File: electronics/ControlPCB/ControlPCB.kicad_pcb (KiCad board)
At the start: 2 copper layers, 119.6 x 90.4 mm, 44 parts, among them CON1 12VINPUT, P1 Opto1, P2 Opto2, P3 Opto3, P4 Opto4, P5 Opto5, P6 Opto6, P7 Tool, U1 POLOLU_A4988, U2 POLOLU_A4988, U3 POLOLU_A4988, U4 POLOLU_A4988, U5 POLOLU_A4988, U6 POLOLU_A4988, U7 POLOLU_A4988

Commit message: PCB update
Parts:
- removed REF**: Symbol_OSHW-Logo_CopperTop_BIG, Symbols:Symbol_OSHW-Logo_CopperTop_BIG
- removed REF** (x4): 1pin, Connect:1pin
- added C8: CP1_Small, Capacitors_SMD:c_elec_6.3x5.7, F.Cu at (166.6, 91.4)
- added D1: D_Small, Diodes_ThroughHole:Diode_DO-35_SOD27_Horizontal_RM10, F.Cu at (85.3, 91.2)
- added DLED1: LEDFAN, LEDs:LED_1206, F.Cu at (100.7, 54.2)
- added DLED2: LED12V, LEDs:LED_1206, F.Cu at (93.3, 54.2)
- added DLED3: LED5V, LEDs:LED_1206, F.Cu at (107.8, 54.2)
- added F1: F_Small, Fuse_Holders_and_Fuses:Fuse_TE5_Littlefuse-395Series, F.Cu at (81.0, 96.0)
- added P8: CONN_02X03, Pin_Headers:Pin_Header_Straight_2x03, F.Cu at (158.8, 87.6)
- added PM8: CONN_01X04, Pin_Headers:Pin_Header_Straight_1x04, F.Cu at (165.1, 100.6)
- added PS1: Opto1, Pin_Headers:Pin_Header_Straight_1x03, F.Cu at (141.4, 49.9)
- added PS2: Opto2, Pin_Headers:Pin_Header_Straight_1x03, F.Cu at (144.9, 49.9)
- added PS3: Opto3, Pin_Headers:Pin_Header_Straight_1x03, F.Cu at (148.5, 49.9)
- added PS4: Opto4, Pin_Headers:Pin_Header_Straight_1x03, F.Cu at (152.0, 49.9)
- added PS5: Opto5, Pin_Headers:Pin_Header_Straight_1x03, F.Cu at (155.6, 49.9)
- added PS6: Opto6, Pin_Headers:Pin_Header_Straight_1x03, F.Cu at (159.1, 49.9)
- added PS7: Opto7, Pin_Headers:Pin_Header_Straight_1x03, F.Cu at (162.7, 49.9)
- added PS8: Opto8, Pin_Headers:Pin_Header_Straight_1x03, F.Cu at (166.2, 49.9)
- added PSW1: CONN_01X02, Connect:AK300-2, F.Cu at (82.8, 84.3)
- added PT1: Tool, Pin_Headers:Pin_Header_Straight_1x03, F.Cu at (169.8, 49.9)
- added R10: R, Resistors_SMD:R_1206_HandSoldering, F.Cu at (117.1, 72.1)
- added R11: R, Resistors_SMD:R_1206_HandSoldering, F.Cu at (137.4, 72.1)
- added R12: R, Resistors_SMD:R_1206_HandSoldering, F.Cu at (157.7, 72.1)
- added R13: R, Resistors_SMD:R_1206_HandSoldering, F.Cu at (96.8, 93.7)
- added R14: R, Resistors_SMD:R_1206_HandSoldering, F.Cu at (117.1, 93.7)
- added R15: R, Resistors_SMD:R_1206_HandSoldering, F.Cu at (137.4, 93.7)
- added R16: R, Resistors_SMD:R_1206_HandSoldering, F.Cu at (157.7, 93.7)
- added R8: R, Resistors_SMD:R_1206_HandSoldering, F.Cu at (167.6, 86.4)
- added R9: R, Resistors_SMD:R_1206_HandSoldering, F.Cu at (96.8, 72.1)
- added RLED1: 560, Resistors_SMD:R_1206_HandSoldering, F.Cu at (100.7, 50.7)
- added RLED2: 560, Resistors_SMD:R_1206_HandSoldering, F.Cu at (93.3, 50.7)
- added RLED3: 220, Resistors_SMD:R_1206_HandSoldering, F.Cu at (107.8, 50.7)
- added U8: POLOLU_A4988, Pololu:SWDIP8_.6W, F.Cu at (161.3, 90.2)
- C1, C2, C3, C4, C5, C6, C7: footprint POL:C_Radial_D6.3_L11.2_P2.5THOR -> Capacitors_SMD:c_elec_6.3x5.7
- P1: value Opto1 -> CONN_02X03; footprint Pin_Header_Straight_1x03 -> Pin_Headers:Pin_Header_Straight_2x03
- P2: value Opto2 -> CONN_02X03; footprint POL:Pin_Header_Straight_1x03 -> Pin_Headers:Pin_Header_Straight_2x03
- P3: value Opto3 -> CONN_02X03; footprint POL:Pin_Header_Straight_1x03 -> Pin_Headers:Pin_Header_Straight_2x03
- P4: value Opto4 -> CONN_02X03; footprint POL:Pin_Header_Straight_1x03 -> Pin_Headers:Pin_Header_Straight_2x03
- P5: value Opto5 -> CONN_02X03; footprint POL:Pin_Header_Straight_1x03 -> Pin_Headers:Pin_Header_Straight_2x03
- P6: value Opto6 -> CONN_02X03; footprint POL:Pin_Header_Straight_1x03 -> Pin_Headers:Pin_Header_Straight_2x03
- P7: value Tool -> CONN_02X03; footprint POL:Pin_Header_Straight_1x03 -> Pin_Headers:Pin_Header_Straight_2x03
- PA1: footprint POL:Pin_Header_Straight_2x03 -> Pin_Headers:Pin_Header_Straight_2x10
- PA2: footprint POL:Pin_Header_Straight_2x03 -> Pin_Headers:Pin_Header_Straight_2x03
- PDIG1: footprint POL:Pin_Header_Straight_2x18 -> Pin_Headers:Pin_Header_Straight_2x18
- PM1, PM2, PM3, PM4, PM5, PM6, PM7: footprint POL:Pin_Header_Straight_1x04 -> Pin_Headers:Pin_Header_Straight_1x04
- R1, R2, R3, R4, R5, R6, R7: footprint POL:Resistor_Horizontal_RM7mm -> Resistors_SMD:R_1206_HandSoldering
- U1, U2, U3, U4, U5, U6, U7: footprint POL:POLA4988 -> Pololu:SWDIP8_.6W
- moved P1 106.7 mm to (97.8, 66.0)
- moved P5 104.9 mm to (97.8, 87.6)
- moved P2 86.1 mm to (118.1, 66.0)
- moved P6 85.3 mm to (118.1, 87.6)
- moved P7 66.4 mm to (138.4, 87.6)
- moved P3 65.5 mm to (138.4, 66.0)
- moved P4 45.0 mm to (158.8, 66.0)
- moved PA1 43.7 mm to (70.9, 57.7), turned to 0 degrees
- moved R6 37.9 mm to (127.0, 86.4), turned to 180 degrees
- moved R7 37.9 mm to (147.3, 86.4), turned to 180 degrees
- moved R5 37.9 mm to (106.7, 86.4), turned to 180 degrees
- moved PA2 37.0 mm to (79.0, 68.1), turned to 0 degrees
- moved U7 33.1 mm to (141.0, 90.2), turned to 0 degrees
- moved U5 33.1 mm to (100.3, 90.2), turned to 0 degrees
- moved U6 33.1 mm to (120.7, 90.2), turned to 0 degrees
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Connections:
- CON1 pad 1: +12V -> Net-(CON1-Pad1)
- P1 pad 1: GND -> VCC
- P1 pad 2: VCC -> Net-(P1-Pad2)
- P1 pad 3: SOPTO1 -> VCC
- P2 pad 1: GND -> VCC
- P2 pad 2: VCC -> Net-(P2-Pad2)
- P2 pad 3: SOPTO2 -> VCC
- P3 pad 1: GND -> VCC
- P3 pad 2: VCC -> Net-(P3-Pad2)
- P3 pad 3: SOPTO3 -> VCC
- P4 pad 1: GND -> VCC
- P4 pad 2: VCC -> Net-(P4-Pad2)
- P4 pad 3: SOPTO4 -> VCC
- P5 pad 1: GND -> VCC
- P5 pad 2: VCC -> Net-(P5-Pad2)
- P5 pad 3: SOPTO5 -> VCC
- P6 pad 1: GND -> VCC
- P6 pad 2: VCC -> Net-(P6-Pad2)
- P6 pad 3: SOPTO6 -> VCC
- P7 pad 1: GND -> VCC
- P7 pad 2: VCC -> Net-(P7-Pad2)
- P7 pad 3: STOOL -> VCC
- PA1 pad 2: +12V -> VDD
- PA1 pad 4: +12V -> VDD
- PA1 pad 6: +12V -> VDD
- PDIG1 pad 10: SOPTO4 -> STEPM8
- PDIG1 pad 11: STEPM3 -> DIRM1
- PDIG1 pad 12: SOPTO3 -> DIRM2
- PDIG1 pad 13: ENABLEM3 -> DIRM3
- PDIG1 pad 14: SOPTO2 -> DIRM4
- PDIG1 pad 15: DIRM2 -> DIRM5
- PDIG1 pad 16: SOPTO1 -> DIRM6
- PDIG1 pad 17: STEPM2 -> DIRM7
- PDIG1 pad 18: Net-(PDIG1-Pad18) -> DIRM8
- PDIG1 pad 19: ENABLEM2 -> Net-(PDIG1-Pad19)
- PDIG1 pad 21: DIRM1 -> ENABLEM
- PDIG1 pad 22: Net-(PDIG1-Pad22) -> STOOL
- PDIG1 pad 23: STEPM1 -> SOPTO1
- PDIG1 pad 24: ENABLEM5 -> SOPTO2
- PDIG1 pad 25: ENABLEM1 -> SOPTO3
- PDIG1 pad 26: STEPM5 -> SOPTO4
- PDIG1 pad 27: DIRM7 -> SOPTO5
- PDIG1 pad 28: DIRM5 -> SOPTO6
- PDIG1 pad 29: STEPM7 -> SOPTO7
- PDIG1 pad 3: DIRM4 -> STEPM1
- PDIG1 pad 30: ENABLEM6 -> SOPTO8
- PDIG1 pad 31: ENABLEM7 -> Net-(PDIG1-Pad31)
- PDIG1 pad 32: STEPM6 -> Net-(PDIG1-Pad32)
- PDIG1 pad 34: DIRM6 -> Net-(PDIG1-Pad34)
- PDIG1 pad 4: STOOL -> STEPM2
- PDIG1 pad 5: STEPM4 -> STEPM3
- PDIG1 pad 6: SOPTO6 -> STEPM4
- PDIG1 pad 7: ENABLEM4 -> STEPM5
- PDIG1 pad 8: SOPTO5 -> STEPM6
- PDIG1 pad 9: DIRM3 -> STEPM7
- R1 pad 1: ENABLEM1 -> ENABLEM
- R2 pad 1: ENABLEM2 -> ENABLEM
- R3 pad 1: ENABLEM3 -> ENABLEM
- R4 pad 1: ENABLEM4 -> ENABLEM
- R5 pad 1: ENABLEM5 -> ENABLEM
- R6 pad 1: ENABLEM6 -> ENABLEM
- R7 pad 1: ENABLEM7 -> ENABLEM
- U1 pad 10: VCC -> Net-(P1-Pad2)
- U1 pad 11: VCC -> Net-(P1-Pad4)
- U1 pad 12: VCC -> Net-(P1-Pad6)
- U1 pad 9: ENABLEM1 -> ENABLEM
- U2 pad 10: VCC -> Net-(P2-Pad2)
- U2 pad 11: VCC -> Net-(P2-Pad4)
- U2 pad 12: VCC -> Net-(P2-Pad6)
- U2 pad 9: ENABLEM2 -> ENABLEM
- U3 pad 10: VCC -> Net-(P3-Pad2)
- U3 pad 11: VCC -> Net-(P3-Pad4)
- U3 pad 12: VCC -> Net-(P3-Pad6)
- U3 pad 9: ENABLEM3 -> ENABLEM
- U4 pad 10: VCC -> Net-(P4-Pad2)
- U4 pad 11: VCC -> Net-(P4-Pad4)
- U4 pad 12: VCC -> Net-(P4-Pad6)
- U4 pad 9: ENABLEM4 -> ENABLEM
- U5 pad 10: VCC -> Net-(P5-Pad2)
- U5 pad 11: VCC -> Net-(P5-Pad4)
- U5 pad 12: VCC -> Net-(P5-Pad6)
- U5 pad 9: ENABLEM5 -> ENABLEM
- U6 pad 10: VCC -> Net-(P6-Pad2)
- U6 pad 11: VCC -> Net-(P6-Pad4)
- U6 pad 12: VCC -> Net-(P6-Pad6)
- U6 pad 9: ENABLEM6 -> ENABLEM
- U7 pad 10: VCC -> Net-(P7-Pad2)
- U7 pad 11: VCC -> Net-(P7-Pad4)
- U7 pad 12: VCC -> Net-(P7-Pad6)
- U7 pad 9: ENABLEM7 -> ENABLEM
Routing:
- net VCC: track 635.6 -> 0.00 mm
- net +12V: track 232.8 -> 0.00 mm
- net ENABLEM5: track 132.0 -> 0.00 mm
- net STEPM5: track 110.1 -> 0.00 mm
- net ENABLEM1: track 103.1 -> 0.00 mm
- net DIRM5: track 99.2 -> 0.00 mm
- net ENABLEM6: track 87.9 -> 0.00 mm
- net STEPM1: track 87.7 -> 0.00 mm
- net DIRM1: track 84.2 -> 0.00 mm
- net ENABLEM2: track 80.9 -> 0.00 mm
- net STEPM2: track 66.7 -> 0.00 mm
- net STEPM6: track 66.3 -> 0.00 mm
- net DIRM2: track 62.8 -> 0.00 mm
- net ENABLEM3: track 59.0 -> 0.00 mm
- net DIRM6: track 54.9 -> 0.00 mm
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- removed copper zone on B.Cu, net GND
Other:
- board outline removed
- net class Default: clearance 0.2 -> 0; trace_width 1.016 -> 0.254; via_dia 0.6 -> 0.6096; via_drill 0.4 -> 0.3048
- rule pad_to_mask_clearance: 0.2 -> 0
- rule trace_clearance: 0.2 -> 0
- rule trace_min: 0.2 -> 0.1524
- rule via_min_drill: 0.3 -> 0.3048
- rule via_min_size: 0.4 -> 0.6096

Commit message: update2
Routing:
- net VDD: track 53.7 -> 43.8 mm
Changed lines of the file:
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@@
     (thickness 1.6)
     (drawings 0)
-    (tracks 23)
+    (tracks 21)
     (zones 0)
     (modules 70)
@@
   (segment (start 76.05014 95.758) (end 78.22184 95.758) (width 3.048) (layer F.Cu) (net 3))
   (segment (start 78.22184 95.758) (end 81.01584 98.552) (width 3.048) (layer F.Cu) (net 3))
-  (segment (start 81.026 93.472) (end 81.026 86.106) (width 3.048) (layer F.Cu) (net 4) (status 400000))
-  (segment (start 81.026 86.106) (end 82.804 84.328) (width 3.048) (layer F.Cu) (net 4) (status 800000))
-  (segment (start 81.026 93.472) (end 81.026 86.106) (width 3.048) (layer B.Cu) (net 4) (status 400000))
-  (segment (start 81.026 86.106) (end 82.804 84.328) (width 3.048) (layer B.Cu) (net 4) (status 800000))
+  (segment (start 81.026 93.472) (end 81.026 86.106) (width 3.048) (layer B.Cu) (net 4))
+  (segment (start 81.026 86.106) (end 82.804 84.328) (width 3.048) (layer B.Cu) (net 4))
   (segment (start 73.406 57.658) (end 73.406 60.198) (width 1.27) (layer B.Cu) (net 4))
   (segment (start 73.406 60.198) (end 73.406 62.738) (width 1.27) (layer B.Cu) (net 4))

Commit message: ControlPCB before square
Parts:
- moved PM1 22.2 mm to (96.5, 58.2), turned to 90 degrees
- moved PM4 22.2 mm to (157.5, 58.2), turned to 90 degrees
- moved PM2 22.2 mm to (116.8, 58.2), turned to 90 degrees
- moved PM3 22.2 mm to (137.2, 58.2), turned to 90 degrees
- moved R5 18.5 mm to (94.0, 99.8), turned to 0 degrees
- moved R6 18.5 mm to (114.3, 99.8), turned to 0 degrees
- moved R7 18.5 mm to (134.6, 99.8), turned to 0 degrees
- moved R8 18.5 mm to (154.9, 99.8), turned to 0 degrees
- moved PM5 16.8 mm to (96.5, 85.6), turned to 90 degrees
- moved PM7 16.8 mm to (137.2, 85.6), turned to 90 degrees
- moved PM8 16.8 mm to (157.5, 85.6), turned to 90 degrees
- moved PM6 16.8 mm to (116.8, 85.6), turned to 90 degrees
- moved R1 14.8 mm to (94.0, 72.4), turned to 0 degrees
- moved R2 14.8 mm to (114.3, 72.4), turned to 0 degrees
- moved R4 14.8 mm to (154.9, 72.4), turned to 0 degrees
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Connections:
- P1 pad 1: VCC -> Net-(P1-Pad1)
- P1 pad 2: Net-(P1-Pad2) -> VCC
- P1 pad 3: VCC -> Net-(P1-Pad3)
- P1 pad 4: Net-(P1-Pad4) -> VCC
- P1 pad 5: VCC -> Net-(P1-Pad5)
- P1 pad 6: Net-(P1-Pad6) -> VCC
- P2 pad 1: VCC -> Net-(P2-Pad1)
- P2 pad 2: Net-(P2-Pad2) -> VCC
- P2 pad 3: VCC -> Net-(P2-Pad3)
- P2 pad 4: Net-(P2-Pad4) -> VCC
- P2 pad 5: VCC -> Net-(P2-Pad5)
- P2 pad 6: Net-(P2-Pad6) -> VCC
- P3 pad 1: VCC -> Net-(P3-Pad1)
- P3 pad 2: Net-(P3-Pad2) -> VCC
- P3 pad 3: VCC -> Net-(P3-Pad3)
- P3 pad 4: Net-(P3-Pad4) -> VCC
- P3 pad 5: VCC -> Net-(P3-Pad5)
- P3 pad 6: Net-(P3-Pad6) -> VCC
- P4 pad 1: VCC -> Net-(P4-Pad1)
- P4 pad 2: Net-(P4-Pad2) -> VCC
- P4 pad 3: VCC -> Net-(P4-Pad3)
- P4 pad 4: Net-(P4-Pad4) -> VCC
- P4 pad 5: VCC -> Net-(P4-Pad5)
- P4 pad 6: Net-(P4-Pad6) -> VCC
- P5 pad 1: VCC -> Net-(P5-Pad1)
- P5 pad 2: Net-(P5-Pad2) -> VCC
- P5 pad 3: VCC -> Net-(P5-Pad3)
- P5 pad 4: Net-(P5-Pad4) -> VCC
- P5 pad 5: VCC -> Net-(P5-Pad5)
- P5 pad 6: Net-(P5-Pad6) -> VCC
- P6 pad 1: VCC -> Net-(P6-Pad1)
- P6 pad 2: Net-(P6-Pad2) -> VCC
- P6 pad 3: VCC -> Net-(P6-Pad3)
- P6 pad 4: Net-(P6-Pad4) -> VCC
- P6 pad 5: VCC -> Net-(P6-Pad5)
- P6 pad 6: Net-(P6-Pad6) -> VCC
- P7 pad 1: VCC -> Net-(P7-Pad1)
- P7 pad 2: Net-(P7-Pad2) -> VCC
- P7 pad 3: VCC -> Net-(P7-Pad3)
- P7 pad 4: Net-(P7-Pad4) -> VCC
- P7 pad 5: VCC -> Net-(P7-Pad5)
- P7 pad 6: Net-(P7-Pad6) -> VCC
- P8 pad 1: VCC -> Net-(P8-Pad1)
- P8 pad 2: Net-(P8-Pad2) -> VCC
- P8 pad 3: VCC -> Net-(P8-Pad3)
- P8 pad 4: Net-(P8-Pad4) -> VCC
- P8 pad 5: VCC -> Net-(P8-Pad5)
- P8 pad 6: Net-(P8-Pad6) -> VCC
- PDIG1 pad 3: STEPM1 -> STEPM4
- PDIG1 pad 4: STEPM2 -> STEPM5
- PDIG1 pad 6: STEPM4 -> STEPM6
- PDIG1 pad 7: STEPM5 -> STEPM2
- PDIG1 pad 8: STEPM6 -> STEPM7
- PDIG1 pad 9: STEPM7 -> STEPM1
- R10 pad 1: Net-(P2-Pad2) -> Net-(P2-Pad5)
- R11 pad 1: Net-(P3-Pad2) -> Net-(P3-Pad5)
- R12 pad 1: Net-(P4-Pad2) -> Net-(P4-Pad5)
- R13 pad 1: Net-(P5-Pad2) -> Net-(P5-Pad5)
- R14 pad 1: Net-(P6-Pad2) -> Net-(P6-Pad5)
- R15 pad 1: Net-(P7-Pad2) -> Net-(P7-Pad5)
- R16 pad 1: Net-(P8-Pad2) -> Net-(P8-Pad5)
- R9 pad 1: Net-(P1-Pad2) -> Net-(P1-Pad5)
- U1 pad 10: Net-(P1-Pad2) -> Net-(P1-Pad5)
- U1 pad 11: Net-(P1-Pad4) -> Net-(P1-Pad3)
- U1 pad 12: Net-(P1-Pad6) -> Net-(P1-Pad1)
- U2 pad 10: Net-(P2-Pad2) -> Net-(P2-Pad5)
- U2 pad 11: Net-(P2-Pad4) -> Net-(P2-Pad3)
- U2 pad 12: Net-(P2-Pad6) -> Net-(P2-Pad1)
- U3 pad 10: Net-(P3-Pad2) -> Net-(P3-Pad5)
- U3 pad 11: Net-(P3-Pad4) -> Net-(P3-Pad3)
- U3 pad 12: Net-(P3-Pad6) -> Net-(P3-Pad1)
- U4 pad 10: Net-(P4-Pad2) -> Net-(P4-Pad5)
- U4 pad 11: Net-(P4-Pad4) -> Net-(P4-Pad3)
- U4 pad 12: Net-(P4-Pad6) -> Net-(P4-Pad1)
- U5 pad 10: Net-(P5-Pad2) -> Net-(P5-Pad5)
- U5 pad 11: Net-(P5-Pad4) -> Net-(P5-Pad3)
- U5 pad 12: Net-(P5-Pad6) -> Net-(P5-Pad1)
- U6 pad 10: Net-(P6-Pad2) -> Net-(P6-Pad5)
- U6 pad 11: Net-(P6-Pad4) -> Net-(P6-Pad3)
- U6 pad 12: Net-(P6-Pad6) -> Net-(P6-Pad1)
- U7 pad 10: Net-(P7-Pad2) -> Net-(P7-Pad5)
- U7 pad 11: Net-(P7-Pad4) -> Net-(P7-Pad3)
- U7 pad 12: Net-(P7-Pad6) -> Net-(P7-Pad1)
- U8 pad 10: Net-(P8-Pad2) -> Net-(P8-Pad5)
- U8 pad 11: Net-(P8-Pad4) -> Net-(P8-Pad3)
- U8 pad 12: Net-(P8-Pad6) -> Net-(P8-Pad1)
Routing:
- net VCC: track 0.00 -> 523.0 mm
- net GND: track 0.00 -> 303.0 mm
- net ENABLEM: track 0.00 -> 227.2 mm
- net +12V: track 0.00 -> 219.6 mm
- net STEPM5: track 0.00 -> 118.7 mm
- net STEPM6: track 0.00 -> 95.8 mm
- net STEPM1: track 0.00 -> 80.9 mm
- net STEPM7: track 0.00 -> 70.6 mm
- net STEPM2: track 0.00 -> 61.3 mm
- net STEPM3: track 0.00 -> 42.3 mm
- net STEPM8: track 0.00 -> 42.3 mm
- net Net-(P1-Pad5): track 0.00 -> 34.6 mm
- net Net-(P1-Pad1): track 0.00 -> 22.4 mm
- net VDD: track 43.8 -> 65.2 mm
- net Net-(P1-Pad3): track 0.00 -> 21.2 mm
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
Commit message: ControlPCB update
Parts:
- moved PA1 98.4 mm to (130.0, 136.3), turned to 90 degrees
- moved RLED2 92.4 mm to (132.2, 127.3), turned to 270 degrees
- moved PA2 92.4 mm to (147.8, 129.7), turned to 90 degrees
- moved RLED1 91.6 mm to (137.4, 127.3), turned to 270 degrees
- moved PS1 91.1 mm to (162.4, 133.7), turned to 180 degrees
- moved PS2 91.1 mm to (166.0, 133.7), turned to 180 degrees
- moved PS3 91.1 mm to (169.5, 133.7), turned to 180 degrees
- moved PS4 91.1 mm to (173.1, 133.7), turned to 180 degrees
- moved PS5 91.1 mm to (176.7, 133.7), turned to 180 degrees
- moved PS6 91.1 mm to (180.2, 133.7), turned to 180 degrees
- moved PS7 91.1 mm to (183.8, 133.7), turned to 180 degrees
- moved PS8 91.1 mm to (187.3, 133.7), turned to 180 degrees
- moved RLED3 90.9 mm to (142.6, 127.3), turned to 270 degrees
- moved PT1 88.3 mm to (158.2, 133.7), turned to 180 degrees
- moved DLED2 88.2 mm to (129.7, 127.3), turned to 90 degrees
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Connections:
- PDIG1 pad 11: DIRM1 -> DIRM4
- PDIG1 pad 12: DIRM2 -> DIRM5
- PDIG1 pad 14: DIRM4 -> DIRM6
- PDIG1 pad 15: DIRM5 -> DIRM2
- PDIG1 pad 16: DIRM6 -> DIRM7
- PDIG1 pad 17: DIRM7 -> DIRM1
- PDIG1 pad 24: SOPTO2 -> SOPTO8
- PDIG1 pad 25: SOPTO3 -> SOPTO2
- PDIG1 pad 26: SOPTO4 -> SOPTO7
- PDIG1 pad 27: SOPTO5 -> SOPTO3
- PDIG1 pad 29: SOPTO7 -> SOPTO4
- PDIG1 pad 30: SOPTO8 -> SOPTO5
- PDIG1 pad 35: GND -> Net-(PDIG1-Pad35)
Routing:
- net GND: track 303.0 -> 550.2 mm
- net VCC: track 523.0 -> 631.9 mm, vias 0 -> 2
- net DIRM5: track 0.00 -> 102.5 mm
- net +12V: track 219.6 -> 319.4 mm
- net ENABLEM: track 227.2 -> 320.2 mm, vias 0 -> 2
- net DIRM6: track 0.00 -> 79.2 mm
- net DIRM1: track 0.00 -> 68.8 mm
- net DIRM7: track 0.00 -> 54.9 mm
- net STOOL: track 0.00 -> 48.6 mm
- net DIRM2: track 0.00 -> 47.5 mm
- net SOPTO1: track 0.00 -> 40.4 mm
- net SOPTO2: track 0.00 -> 34.2 mm
- net SOPTO3: track 0.00 -> 28.2 mm
- net DIRM8: track 0.00 -> 27.6 mm
- net DIRM3: track 0.00 -> 26.9 mm
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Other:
- board outline added: 99.8 x 67.4 mm
- net class Default: clearance 0 -> 0.0762
- rule trace_clearance: 0 -> 0.0762
- rule via_min_size: 0.6096 -> 0.3048

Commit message: ControlPCB update
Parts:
- removed CON1: 12VINPUT, Connect:BARREL_JACK
- added PIN1: CONN_01X02, Molex2:Conn2, F.Cu at (98.2, 133.3)
- F1: footprint Fuse_Holders_and_Fuses:Fuse_TE5_Littlefuse-395Series -> Fuse_TE5_Littlefuse-395Series
- PSW1: footprint Connect:AK300-2 -> Molex2:Conn2
- moved F1 2.59 mm to (106.0, 132.0)
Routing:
- net GND: track 550.2 -> 528.0 mm
- net VDD: track 77.8 -> 73.7 mm
- net +12V: track 319.4 -> 321.5 mm
- net Net-(F1-Pad2): track 12.2 -> 13.6 mm

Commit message: mistakes were made
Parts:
- moved PSW1 9.14 mm to (110.9, 133.9), turned to 180 degrees
- moved F1 5.36 mm to (104.9, 126.7), turned to 180 degrees
- moved D1 4.84 mm to (115.8, 127.3)
- moved PIN1 1.61 mm to (99.7, 133.9), turned to 180 degrees
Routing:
- net GND: track 528.0 -> 570.7 mm, vias 0 -> 1
- net +12V: track 321.5 -> 319.9 mm, vias 0 -> 1
- net VDD: track 73.7 -> 74.5 mm
- net Net-(F1-Pad2): track 13.6 -> 14.3 mm
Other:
- board size 99.8 x 67.4 mm -> 99.8 x 68.5 mm

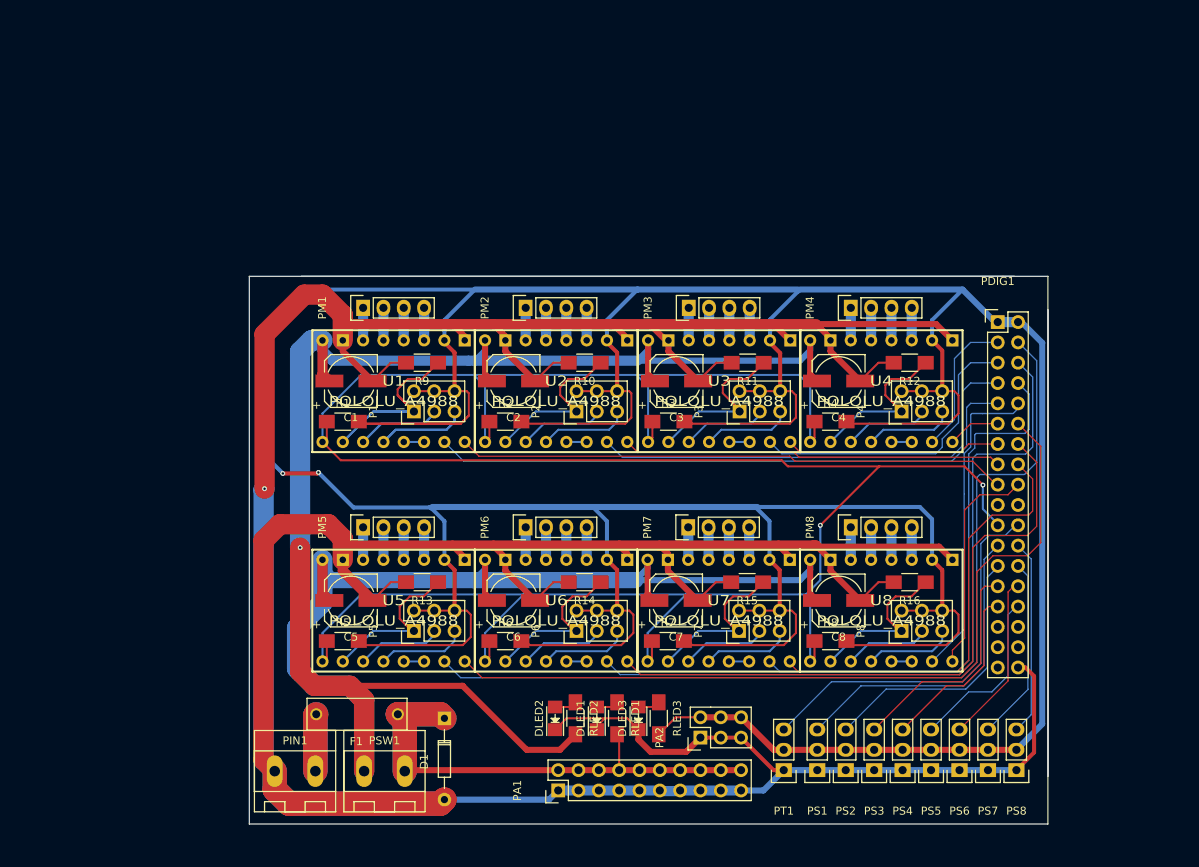
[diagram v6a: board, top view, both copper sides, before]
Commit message: ControlPCB silkscreen cleaned!
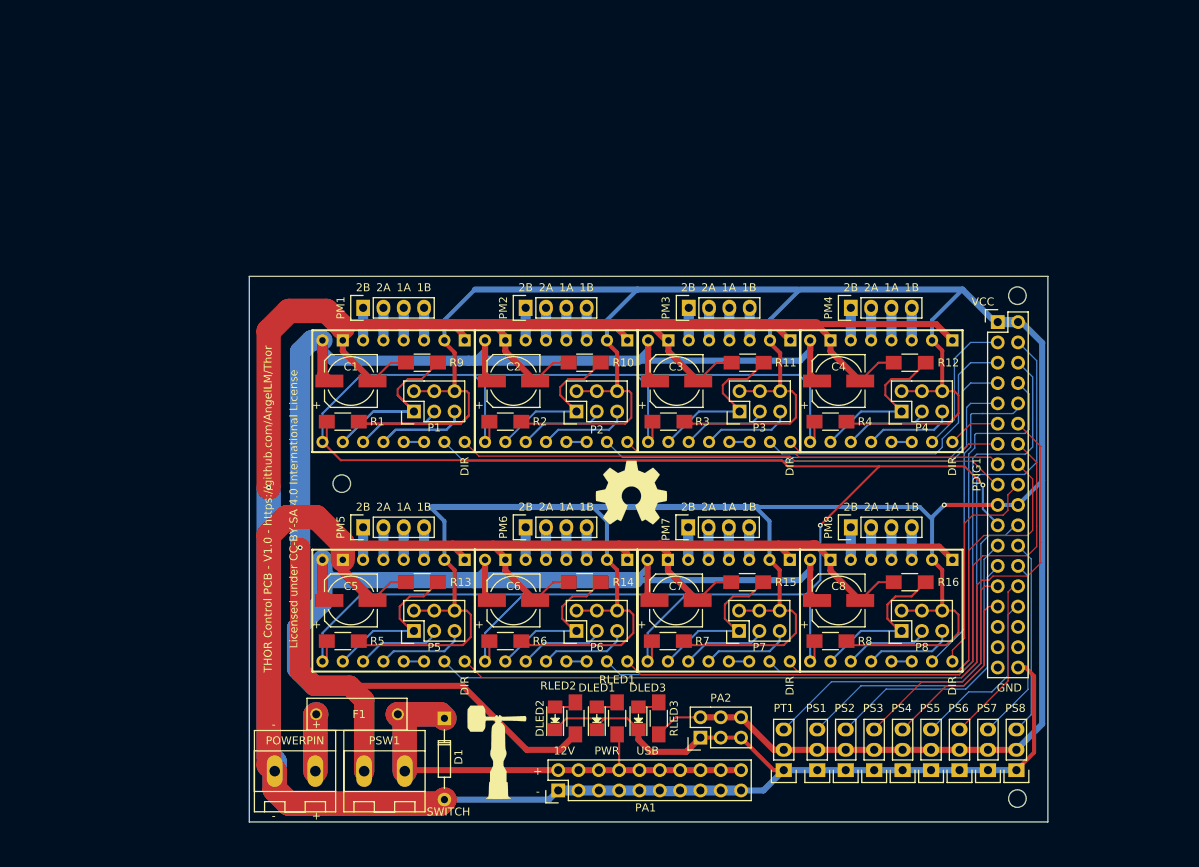
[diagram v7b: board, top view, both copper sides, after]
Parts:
- added G***: LOGO, ThorLogo:ThorLogo, F.Cu at (203.3, 110.0)
- added G***: LOGO, ThorLogo:ThorLogo, F.Cu at (122.4, 131.5)
- added REF**: MountingHole_2.2mm_M2, Mounting_Holes:MountingHole_2.2mm_M2, F.Cu at (103.0, 97.9)
- added REF**: MountingHole_2.2mm_M2, Mounting_Holes:MountingHole_2.2mm_M2, F.Cu at (187.5, 137.3)
- added REF**: MountingHole_2.2mm_M2, Mounting_Holes:MountingHole_2.2mm_M2, F.Cu at (187.5, 74.4)
- added REF***: OSHW-Symbol_8.9x8mm_SilkScreen, Symbols:OSHW-Symbol_8.9x8mm_SilkScreen, F.Cu at (139.2, 99.1)
- renumbered PIN1 to POWERPIN
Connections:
- F1 pad 2: Net-(F1-Pad2) -> Net-(CON1-Pad1)
- PDIG1 pad 19: Net-(PDIG1-Pad19) -> VCC
- PDIG1 pad 20: Net-(PDIG1-Pad20) -> VCC
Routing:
- net VCC: track 631.9 -> 580.9 mm, vias 2 -> 1
- net GND: track 570.7 -> 566.4 mm
- net DIRM7: track 54.9 -> 55.4 mm
- net DIRM5: track 102.5 -> 103.0 mm
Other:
- board size 99.8 x 68.5 mm -> 99.8 x 68.2 mm
- board text added: "+"
- board text added: "-"
- board text added: "12V"
- board text added: "1A"
- board text added: "1B"
- board text added: "2A"
- board text added: "2B"
- board text added: "DIR"
- board text added: "GND"
- board text added: "PWR"
- board text added: "SWITCH"
- board text added: "THOR Control PCB - V1.0 - https://github.com/AngelLM/Thor Licensed under CC-BY-SA 4.0 International License"
- board text added: "USB"
- board text added: "VCC"

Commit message: Gerber files uploaded
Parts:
- renumbered POWERPIN to POWERPIN1
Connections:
- F1 pad 2: Net-(CON1-Pad1) -> Net-(F1-Pad2)
